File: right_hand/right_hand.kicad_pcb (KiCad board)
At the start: 2 copper layers, 82 parts, among them U1 SW_Push

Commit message: Assign models for right hand
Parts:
- removed Right_Plug1: RJ45, custom:8P8C_942
- added Right_Plug0: RJ45, custom:8P8C_942, F.Cu at (19.5, -19.8)
- A1, BAT_Decouple1, BAT_EN1, BAT_Fuse1, BAT_MIN1, BIN_Pulldown1, Battery_Charger1, Battery_Monitor1, CHRG_Bypass1, CHRG_Decouple1, CHRG_Shunt1, C_{BATT}1, C_{BATT}2, C_{SYS}1, C_{SYS}2, C_{SYS}3, Current_Monitor1, RFB_{H}1, RFB_{L}1, RLIM_Decouple1, RLIM_{H}1, RLIM_{L}1, RNTC_{H}1, RNTC_{L}1, RREG_{H}1, RREG_{L}1, RWIN_{H}1, RWIN_{L}1, R_{HIST}1, R_{ISET}1, R_{Lower}1, R_{OLIM}1, R_{Pullup}1, R_{Store}1, R_{Upper}1, USB_Default_Power_CC1, USB_Default_Power_CC2, VBAT_PASS1, VBUS_Bypass1, VDD_Decouple1, Wired_Interface1: moved to B.Cu
- BAT1: value 1042 -> 1043; footprint snap_magic_footprints:BAT_1042 -> snap_magic_footprints:BAT_1043
- D_{AS}2: renamed from D_{R}1; moved to B.Cu
- D_{AS}3: renamed from D_{R}2; moved to B.Cu
- D_{B}0: renamed from D_{R}9; moved to B.Cu
- D_{D}0: renamed from D_{R}14; moved to B.Cu
- D_{E}0: renamed from D_{R}3; moved to B.Cu
- D_{F}0: renamed from D_{R}4; moved to B.Cu
- D_{G}0: renamed from D_{R}11; moved to B.Cu
- D_{L}0: renamed from D_{R}10; moved to B.Cu
- D_{NUM}1: renamed from D_{R}7; moved to B.Cu
- D_{PR}0: renamed from D_{R}8; moved to B.Cu
- D_{RR}0: renamed from D_{R}5; moved to B.Cu
- D_{S}2: renamed from D_{R}13; moved to B.Cu
- D_{TR}0: renamed from D_{R}12; moved to B.Cu
- D_{U}0: renamed from D_{R}6; moved to B.Cu
- D_{Z}0: renamed from D_{R}15; moved to B.Cu
- moved BAT_EN1 187.9 mm to (370.0, 33.8), turned to 180 degrees
- moved Asterisk3 170.6 mm to (132.4, -56.5)
- moved B0 170.6 mm to (132.4, -41.0)
- moved F0 170.6 mm to (148.0, -56.5)
- moved G0 170.6 mm to (148.0, -41.0)
- moved Number_Bar11 170.6 mm to (179.1, -56.5)
- moved Number_Bar7 170.6 mm to (163.5, -56.5)
- moved Number_Bar8 170.6 mm to (163.5, -41.0)
- moved P_{R}0 170.6 mm to (179.1, -41.0)
- moved T_{R}0 170.6 mm to (194.6, -56.5)
- moved U0 170.6 mm to (194.6, -41.0)
- moved Asterisk2 170.6 mm to (132.4, -72.1)
- moved D0 170.6 mm to (132.4, -25.4)
- moved E0 170.6 mm to (148.0, -72.1)
- moved L0 170.6 mm to (148.0, -25.4)
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- renumbered Asterisk1 to Asterisk2, Asterisk2 to Asterisk3, B1 to B0, D1 to D0, E1 to E0, F1 to F0, G1 to G0, L1 to L0, Number_Bar5 to Number_Bar10, Number_Bar6 to Number_Bar11, Number_Bar1 to Number_Bar6, Number_Bar2 to Number_Bar7, Number_Bar3 to Number_Bar8, Number_Bar4 to Number_Bar9, P_{R}1 to P_{R}0, R_{R}1 to R_{R}0, S1 to S2, T_{R}1 to T_{R}0, U1 to U0, Z1 to Z0
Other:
- board outline added: 160 x 110 mm

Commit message: Size up components
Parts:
- removed A1: Raspberry Pi Zero v1.3, Raspberry_Pi_Zero_v.1.3_Hat:RASPI_ZERO_FULL
- removed BAT1: 1043, snap_magic_footprints:BAT_1043
- removed BAT_Decouple1: 1uF, Capacitor_SMD:C_0402_1005Metric
- removed BAT_EN1: RA1H1C112R, ultra_librarian_footprints:SW_RA1H1C112R_EWI
- removed BAT_Fuse1: ERB-RE1R00V, ultra_librarian_footprints:FUSE_ERBRE_PAN
- removed BAT_MIN1: DMG2305UX-7, snap_magic_footprints:SOT91P240X110-3N_DMG2305UX-7
- removed BIN_Pulldown1, RNTC_{H}1, RNTC_{L}1, R_{Pullup}1: 10K, Resistor_SMD:R_0402_1005Metric
- removed BT_EN1, STORAGE_EN1, TRANSLATION_EN1: SLW-864587-2A-RA-N-D, snap_magic_footprints:SW_SLW-864587-2A-RA-N-D
- removed Battery_Charger1: MP2637GR-P, ultra_librarian_footprints:QFN-24_MP2637_MNP
- removed Battery_Monitor1: BQ27427YZFR, snap_magic_footprints:IC_BQ27427YZFR
- removed CHRG_Bypass1: 2.2uH, Inductor_SMD:L_1210_3225Metric
- removed CHRG_Decouple1: 47nF, Capacitor_SMD:C_0402_1005Metric
- removed CHRG_Shunt1: 20m, Resistor_SMD:R_0805_2012Metric
- removed C_{BATT}1, C_{BATT}2, C_{SYS}1, C_{SYS}2, C_{SYS}3, VBUS_Bypass1: 22uF, Capacitor_SMD:C_1206_3216Metric
- removed Current_Monitor1: MCP3204T-CI/SL, ultra_librarian_footprints:SOIC14-N_MC_MCH
- removed RFB_{H}1: 31.6k, Resistor_SMD:R_0402_1005Metric
- removed RFB_{L}1, RLIM_{H}1: 10k, Resistor_SMD:R_0402_1005Metric
- removed RLIM_Decouple1: 0.1uF, Capacitor_SMD:C_0201_0603Metric
- removed RLIM_{L}1: MCP40D19T-104E_LT, snap_magic_footprints:SOT65P210X110-5N
- removed RREG_{H}1: 15k, Resistor_SMD:R_0805_2012Metric
- removed RREG_{L}1, RWIN_{L}1: 5.1k, Resistor_SMD:R_0603_1608Metric
- removed RWIN_{H}1: 21.5k, Resistor_SMD:R_0603_1608Metric
- removed R_{HIST}1: 500K, Resistor_SMD:R_0805_2012Metric
- removed R_{ISET}1: 73.2k, Resistor_SMD:R_0402_1005Metric
- removed R_{Lower}1: 4.02K, Resistor_SMD:R_0603_1608Metric
- removed R_{OLIM}1: 590k, Resistor_SMD:R_0603_1608Metric
- removed R_{Store}1: 8.06k, Resistor_SMD:R_0402_1005Metric
- removed R_{Upper}1: 7.15K, Resistor_SMD:R_0603_1608Metric
- removed STORE_EN1: EG2208, snap_magic_footprints:SW_EG2208
- removed USB_Default_Power_CC1, USB_Default_Power_CC2: 5.1K, Resistor_SMD:R_0603_1608Metric
- removed VBAT_PASS1: TLV431BIDBZR, ultra_librarian_footprints:DBZ3
- removed VDD_Decouple1: 2.2uF, Capacitor_SMD:C_0402_1005Metric
- removed Wired_Interface1: USB4105-GF-A, snap_magic_footprints:GCT_USB4105-GF-A

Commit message: Place right hand keys
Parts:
- moved D_{Z}0 252.7 mm to (228.3, 112.4), turned to -90 degrees
- moved D_{D}0 250.9 mm to (228.3, 93.3), turned to -90 degrees
- moved D_{S}2 234.6 mm to (209.1, 112.5), turned to -90 degrees
- moved D_{TR}0 226.8 mm to (209.0, 93.4), turned to -90 degrees
- moved E0 214.9 mm to (86.7, 133.9)
- moved D_{G}0 202.0 mm to (183.7, 99.8), turned to -90 degrees
- moved D_{L}0 201.4 mm to (183.8, 80.8), turned to -90 degrees
- moved U0 196.2 mm to (105.8, 133.9)
- moved S2 190.2 mm to (201.0, 118.0)
- moved D_{B}0 176.4 mm to (158.5, 87.0), turned to -90 degrees
- moved D_{PR}0 176.2 mm to (158.4, 67.9), turned to -90 degrees
- moved D_{NUM}1 170.3 mm to (150.2, 43.2)
- moved Asterisk3 164.0 mm to (105.8, 105.3)
- moved Asterisk2 160.6 mm to (105.8, 86.2)
- moved T_{R}0 155.6 mm to (201.0, 99.0)
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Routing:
- net /Control/Right_Columns1: track 0.00 -> 71.8 mm
- net /Control/Right_Columns3: track 0.00 -> 58.4 mm
- net /Control/Right_Columns4: track 0.00 -> 58.3 mm
- net /Control/Right_Columns0: track 0.00 -> 39.8 mm
- net /Control/Right_Columns2: track 0.00 -> 20.6 mm
- net Net-(D_{B}0-A): track 0.00 -> 6.02 mm
- net Net-(D_{F}0-A): track 0.00 -> 5.99 mm
- net Net-(D_{E}0-A): track 0.00 -> 5.98 mm
- net Net-(D_{Z}0-A): track 0.00 -> 5.98 mm
- net Net-(D_{U}0-A): track 0.00 -> 5.97 mm
- net Net-(D_{L}0-A): track 0.00 -> 5.92 mm
- net Net-(D_{AS}2-A): track 0.00 -> 5.90 mm
- net Net-(D_{D}0-A): track 0.00 -> 5.89 mm
- net Net-(D_{S}2-A): track 0.00 -> 5.87 mm
- net Net-(D_{PR}0-A): track 0.00 -> 5.84 mm
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
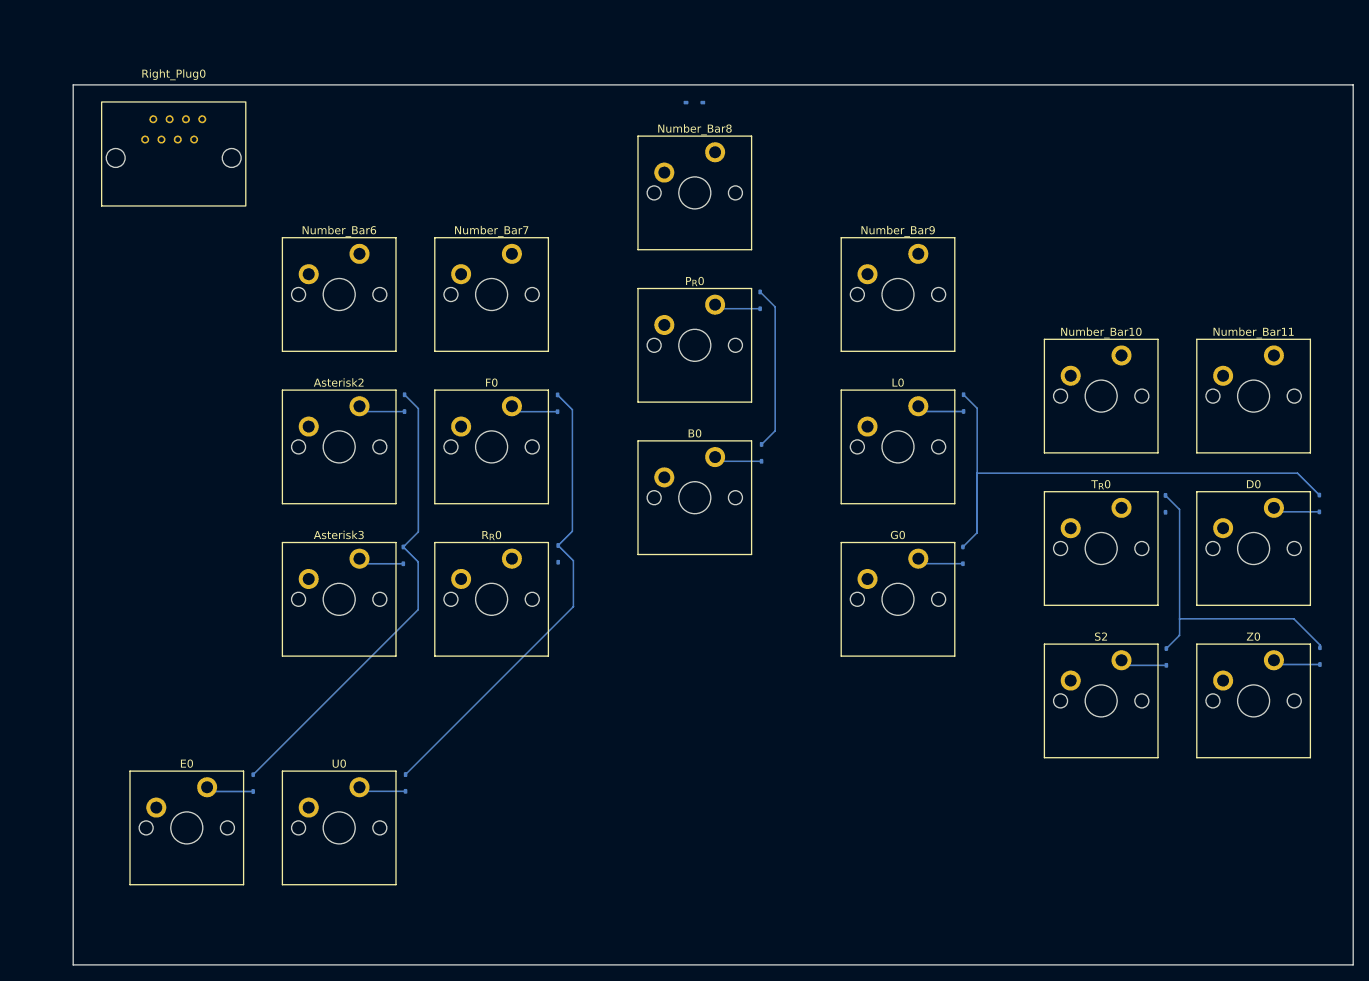
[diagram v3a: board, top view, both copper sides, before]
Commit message: Complete most of RHS layout
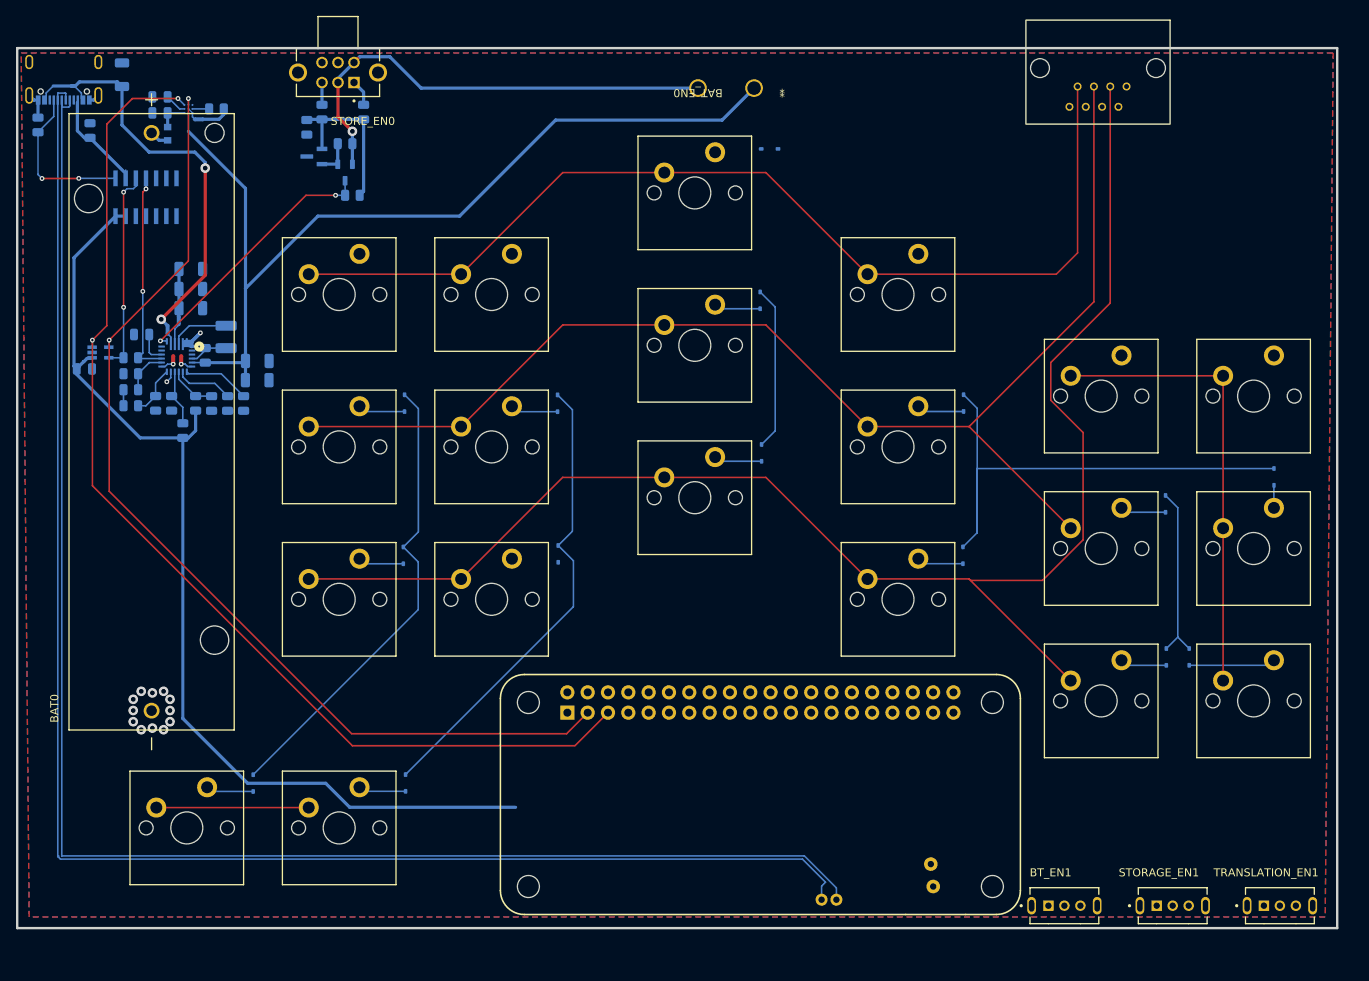
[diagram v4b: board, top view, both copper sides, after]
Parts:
- added A1: Raspberry Pi Zero v1.3, Raspberry_Pi_Zero_v.1.3_Hat:RASPI_ZERO_FULL, B.Cu at (190.9, 144.7)
- added BAT0: 1043, snap_magic_footprints:BAT_1043, F.Cu at (82.3, 83.1)
- added BAT_Decouple0: 1uF, Capacitor_SMD:C_0805_2012Metric, B.Cu at (83.3, 44.5)
- added BAT_EN0: RA1H1C112R, ultra_librarian_footprints:SW_RA1H1C112R_EWI, F.Cu at (157.6, 41.4)
- added BAT_Fuse0: ERB-RE1R00V, ultra_librarian_footprints:FUSE_ERBRE_PAN, B.Cu at (84.3, 47.1)
- added BAT_MIN0: DMG2305UX-7, snap_magic_footprints:SOT91P240X110-3N_DMG2305UX-7, B.Cu at (106.5, 52.0)
- added BIN_Pulldown0: 10K, Resistor_SMD:R_0805_2012Metric, B.Cu at (90.4, 44.0)
- added BT_EN1: SLW-864587-2A-RA-N-D, snap_magic_footprints:SW_SLW-864587-2A-RA-N-D, F.Cu at (196.4, 143.6)
- added Battery_Charger0: MP2637GR-P, ultra_librarian_footprints:QFN-24_MP2637_MNP, B.Cu at (85.5, 75.0)
- added Battery_Monitor0: BQ27427YZFR, snap_magic_footprints:IC_BQ27427YZFR, B.Cu at (86.9, 44.0)
- added CHRG_Bypass0: 2.2uH, Inductor_SMD:L_1210_3225Metric, B.Cu at (91.6, 72.5)
- added CHRG_Decouple0: 47nF, Capacitor_SMD:C_0805_2012Metric, B.Cu at (81.0, 72.2)
- added CHRG_Shunt0: 20m, Resistor_SMD:R_0805_2012Metric, B.Cu at (89.0, 74.8)
- added C_{BATT}0: 22uF, Capacitor_SMD:C_1206_3216Metric, B.Cu at (95.5, 77.9)
- added C_{BATT}1: 22uF, Capacitor_SMD:C_1206_3216Metric, B.Cu at (95.5, 75.5)
- added C_{SYS}0: 22uF, Capacitor_SMD:C_1206_3216Metric, B.Cu at (87.2, 68.9)
- added C_{SYS}1: 22uF, Capacitor_SMD:C_1206_3216Metric, B.Cu at (87.2, 66.5)
- added C_{SYS}2: 22uF, Capacitor_SMD:C_1206_3216Metric, B.Cu at (87.2, 64.0)
- added Current_Monitor1: MCP3204T-CI/SL, ultra_librarian_footprints:SOIC14-N_MC_MCH, B.Cu at (81.6, 55.0)
- added NT0: NetTie_2, NetTie:NetTie-2_SMD_Pad0.5mm, B.Cu at (85.7, 70.4)
- added NT1: NetTie_2, NetTie:NetTie-2_SMD_Pad0.5mm, B.Cu at (84.3, 71.6)
- added NT2: NetTie_2, NetTie:NetTie-2_SMD_Pad0.5mm, B.Cu at (88.2, 45.3)
- added NT3: NetTie_2, NetTie:NetTie-2_SMD_Pad0.5mm, F.Cu at (85.0, 75.4)
- added NT4: NetTie_2, NetTie:NetTie-2_SMD_Pad0.5mm, F.Cu at (86.0, 75.4)
- added RFB_{H}0: 31.6k, Resistor_SMD:R_0805_2012Metric, B.Cu at (86.2, 84.2)
- added RFB_{L}0: 10k, Resistor_SMD:R_0805_2012Metric, B.Cu at (84.8, 80.8)
- added RLIM_Decouple0: 0.1uF, Capacitor_SMD:C_0805_2012Metric, B.Cu at (73.9, 76.5)
- added RLIM_{H}0: 10k, Resistor_SMD:R_0805_2012Metric, B.Cu at (79.7, 75.1)
- added RLIM_{L}0: MCP40D19T-104E_LT, snap_magic_footprints:SOT65P210X110-5N, B.Cu at (75.9, 74.4)
- added RNTC_{H}0: 10k, Resistor_SMD:R_0805_2012Metric, B.Cu at (87.8, 80.8)
- added RNTC_{L}0: 10k, Resistor_SMD:R_0805_2012Metric, B.Cu at (89.8, 80.8)
- added RREG_{H}0: 15k, Resistor_SMD:R_0805_2012Metric, B.Cu at (79.7, 81.1)
- added RREG_{L}0: 5.1k, Resistor_SMD:R_0805_2012Metric, B.Cu at (82.8, 80.8)
- added RWIN_{H}0: 21.5k, Resistor_SMD:R_0805_2012Metric, B.Cu at (79.7, 79.1)
- added RWIN_{L}0: 5.1k, Resistor_SMD:R_0805_2012Metric, B.Cu at (79.7, 77.1)
- added R_{HIST}0: 500K, Resistor_SMD:R_0805_2012Metric, B.Cu at (107.4, 54.8)
- added R_{ISET}0: 73.2k, Resistor_SMD:R_0805_2012Metric, B.Cu at (91.8, 80.8)
- added R_{Lower}0: 4.02K, Resistor_SMD:R_0805_2012Metric, B.Cu at (101.7, 46.3)
- added R_{OLIM}0: 590k, Resistor_SMD:R_0805_2012Metric, B.Cu at (93.8, 80.8)
- added R_{Pullup}0: 10K, Resistor_SMD:R_0805_2012Metric, B.Cu at (106.5, 48.4)
- added R_{Store}0: 8.06k, Resistor_SMD:R_0805_2012Metric, B.Cu at (108.8, 44.4)
- added R_{Upper}0: 7.15K, Resistor_SMD:R_0805_2012Metric, B.Cu at (103.6, 44.4)
- added STORAGE_EN1: SLW-864587-2A-RA-N-D, snap_magic_footprints:SW_SLW-864587-2A-RA-N-D, F.Cu at (209.9, 143.6)
- added STORE_EN0: EG2208, snap_magic_footprints:SW_EG2208, F.Cu at (105.6, 39.5)
- added TRANSLATION_EN1: SLW-864587-2A-RA-N-D, snap_magic_footprints:SW_SLW-864587-2A-RA-N-D, F.Cu at (223.3, 143.6)
- added USB_Default_Power_CC1: 5.1K, Resistor_SMD:R_0805_2012Metric, B.Cu at (68.1, 46.0)
- added USB_Default_Power_CC2: 5.1K, Resistor_SMD:R_0805_2012Metric, B.Cu at (74.6, 46.7)
- added VBAT_PASS0: TLV431BIDBZR, ultra_librarian_footprints:DBZ3, B.Cu at (102.6, 50.0)
- added VBUS_Bypass0: 22uF, Capacitor_SMD:C_1206_3216Metric, B.Cu at (78.6, 39.7)
- added VDD_Decouple0: 2.2uF, Capacitor_SMD:C_0805_2012Metric, B.Cu at (83.3, 42.5)
- added Wired_Interface1: USB4105-GF-A, snap_magic_footprints:GCT_USB4105-GF-A, B.Cu at (71.3, 38.1)
- moved Right_Plug0 116.0 mm to (200.6, 39.4), turned to 180 degrees
- moved D_{Z}0 16.3 mm to (212.0, 112.5)
- moved D_{NUM}1 11.0 mm to (159.6, 49.0)
- moved D_{D}0 6.57 mm to (222.6, 90.0)
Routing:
- net /Rows2: track 0.00 -> 204.7 mm
- net /Control/Data_N: track 0.00 -> 197.1 mm
- net /Control/Data_P: track 0.00 -> 197.0 mm
- net /Rows1: track 0.00 -> 188.6 mm
- net /Rows0: track 0.00 -> 160.0 mm
- net /Control/SCL: track 0.00 -> 137.8 mm, vias 0 -> 2
- net /Control/V_{SYS}: track 0.00 -> 133.1 mm
- net /Control/SDA: track 0.00 -> 128.4 mm, vias 0 -> 2
- net Net-(Battery_Charger0-BATT): track 0.00 -> 117.1 mm
- net Net-(BAT_EN0-Pad2): track 0.00 -> 60.4 mm, vias 0 -> 1
- net /Interface/Battery/V_{BUS}: track 0.00 -> 56.0 mm, vias 0 -> 2
- net Net-(Battery_Charger0-MODE): track 0.00 -> 33.3 mm, vias 0 -> 2
- net /Interface/Battery/CHRG_DIV_{L}: track 0.00 -> 26.1 mm, vias 0 -> 2
- net /Interface/Battery/CHRG_DIV_{H}: track 0.00 -> 25.7 mm, vias 0 -> 2
- net Net-(VBAT_PASS0-REF): track 0.00 -> 20.5 mm
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- added copper zone on B.Cu, net GND
- added copper zone on F.Cu, net GND
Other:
- board size 160 x 110 mm -> 165 x 110 mm
